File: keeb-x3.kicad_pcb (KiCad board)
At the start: 2 copper layers, 383.4 x 133.3 mm, 220 parts, among them J1 USB_C_Receptacle_USB2.0, J2 hole_1x03_D_0.7mm, SW1 MX-ESC, SW10 MX_F9, SW100 MX_LEFT, SW101 MX_DOWN, SW102 MX_RIGHT, SW103 MX_P0, SW104 MX_P., SW105 MX_PGDOWN, SW11 MX_F10, SW12 MX_F11, SW13 MX_F12, SW14 MX_PrtSc, SW15 MX_Scrlck, SW16 MX_Pause, SW17 MX_Insert, SW18 MX_Delete, SW19 MX-~, SW2 MX_F1, SW20 MX-1, SW21 MX-2, SW22 MX-3, SW23 MX-4, SW24 MX-5, SW25 MX_6, SW26 MX_7, SW27 MX_8, SW28 MX_9, SW29 MX_0, SW3 MX_F2, SW30 MX_-, SW31 MX_=, SW32 MX_backspace, SW33 MX_NLCK(prolly FN), SW34 MX_P/, SW35 MX_P*, SW36 MX_P-, SW37 MX-TAB, SW38 MX-Q, SW39 MX-W, SW4 MX_F3, SW40 MX-E, SW41 MX-R, SW42 MX-T, SW43 MX_Y, SW44 MX_U, SW45 MX_I, SW46 MX_O, SW47 MX_P, SW48 MX_[, SW49 MX_], SW5 MX_F4, SW50 MX_P7, SW51 MX_P8, SW52 MX_P9, SW53 MX_P+, SW54 MX-CAPS, SW55 MX-A, SW56 MX-S, SW57 MX-D, SW58 MX-F, SW59 MX-G, SW6 MX_F5, SW60 MX_H, SW61 MX_J, SW62 MX_K, SW63 MX_L, SW64 MX_;, SW65 MX_', SW66 MX_\, SW67 MX_ENTER, SW68 MX_P4, SW69 MX_P5, SW7 MX_F6, SW70 MX_P6, SW71 MX_PENT, SW72 MX-Lshift, SW73 MX-Z, SW74 MX-X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

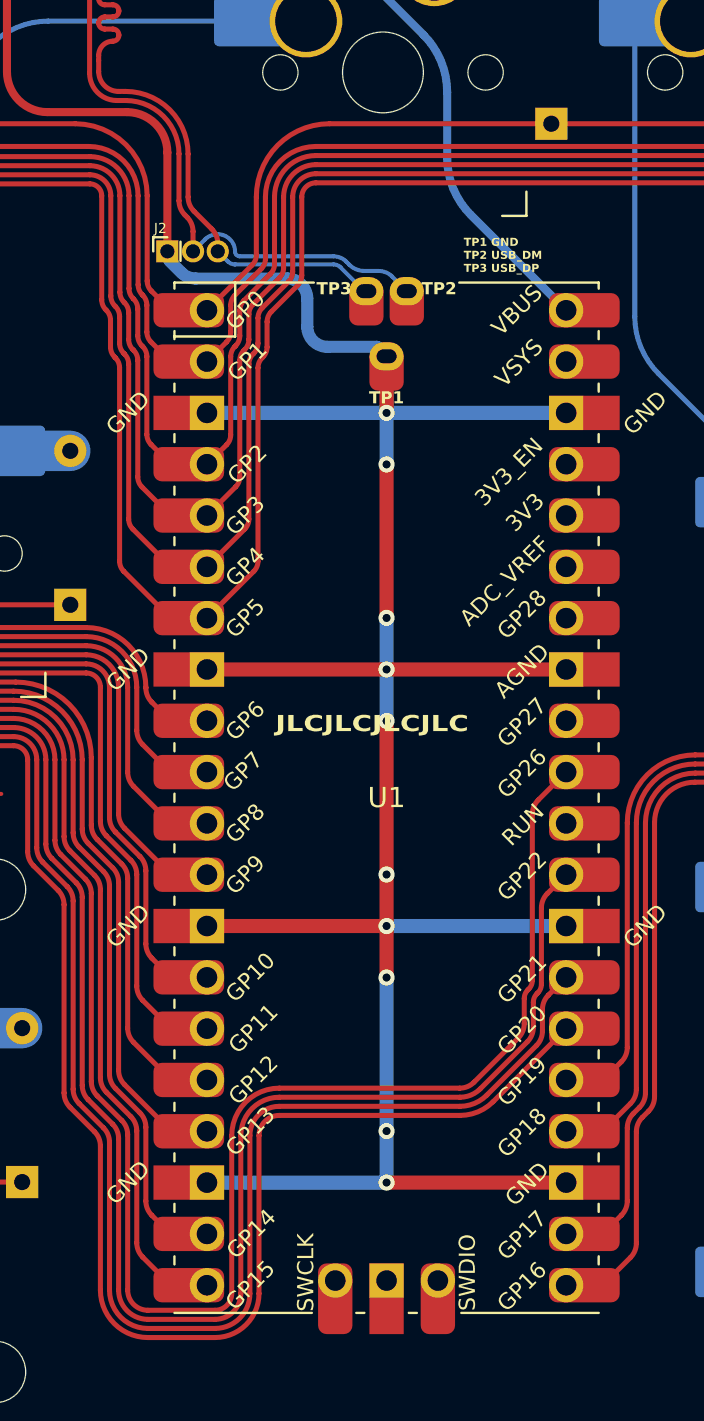
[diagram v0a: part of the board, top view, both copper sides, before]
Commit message: got rid of teardrops on pico to fix clearance issues
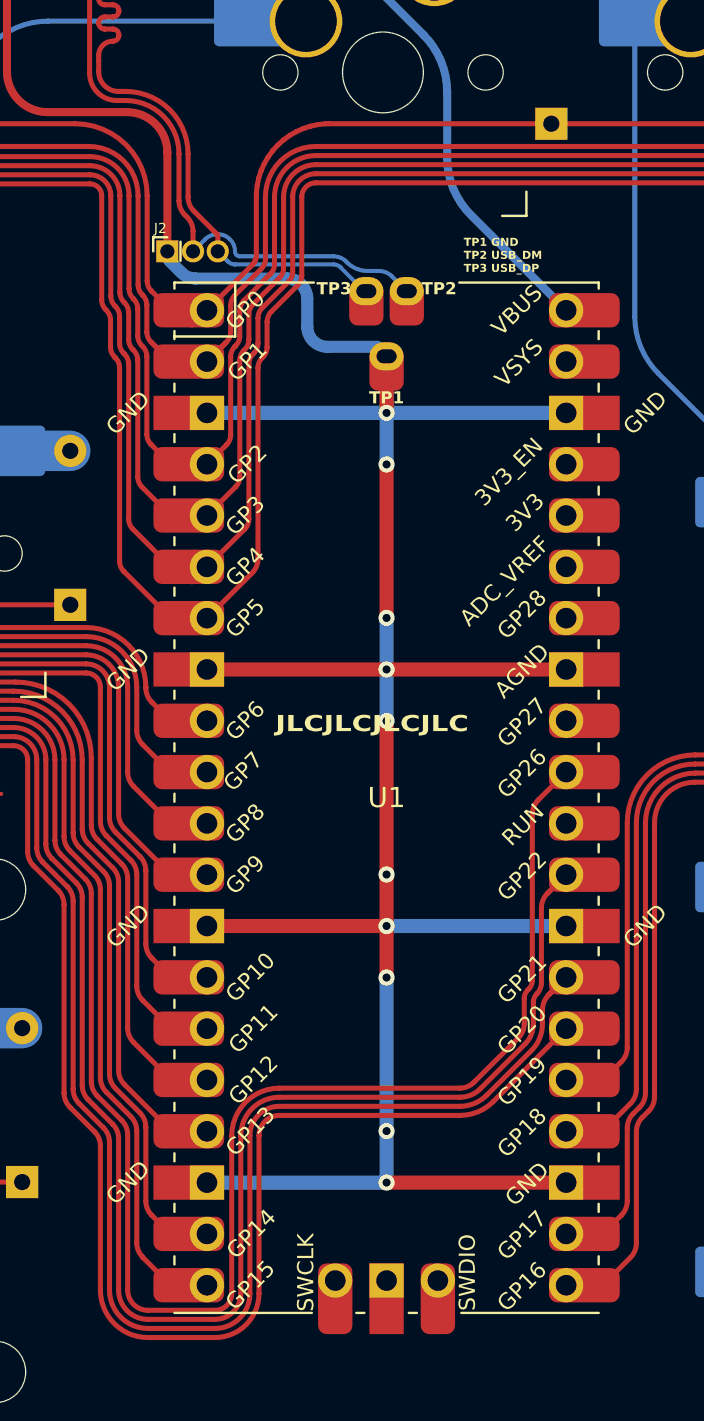
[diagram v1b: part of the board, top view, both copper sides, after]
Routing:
- net Row_5: track 943.5 -> 948.0 mm
- net Col_11: track 196.4 -> 198.6 mm
- net Col_12: track 229.4 -> 231.5 mm
- net Row_1: track 780.1 -> 781.8 mm
- net Row_3: track 853.4 -> 854.9 mm
- net Row_0: track 370.1 -> 371.3 mm
- net Row_2: track 792.2 -> 793.2 mm
- net Row_4: track 903.1 -> 904.1 mm
- net Col_10: track 287.1 -> 288.1 mm
- net Col_13: track 211.8 -> 212.7 mm
- net Col_4: track 334.9 -> 335.8 mm
- net Col_9: track 268.9 -> 269.7 mm

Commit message: last(maybe) pcb revision before attempting a V2 branch
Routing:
- net Row_4: track 904.1 -> 911.5 mm
- net GND: track 151.9 -> 148.2 mm, vias 10 -> 8
- net Row_5: track 948.0 -> 944.6 mm
- net Row_1: track 781.8 -> 778.9 mm
- net Col_11: track 198.6 -> 196.4 mm
- net Col_12: track 231.5 -> 229.4 mm
- net Col_10: track 288.1 -> 287.1 mm
- net Col_13: track 212.7 -> 211.8 mm
- net Col_4: track 335.8 -> 334.9 mm
- net Row_3: track 854.9 -> 854.0 mm
